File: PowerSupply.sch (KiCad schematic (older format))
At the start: 7 parts, among them P1 USB_OTG, P2 CONN_01X03, U1 LM3671MF-3.3

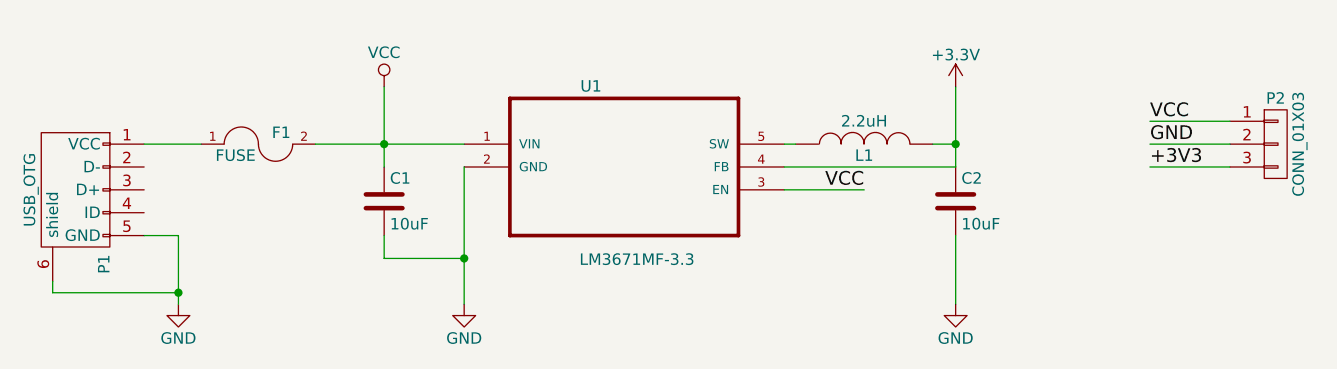
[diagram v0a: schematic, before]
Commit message: Adds Power-on LED
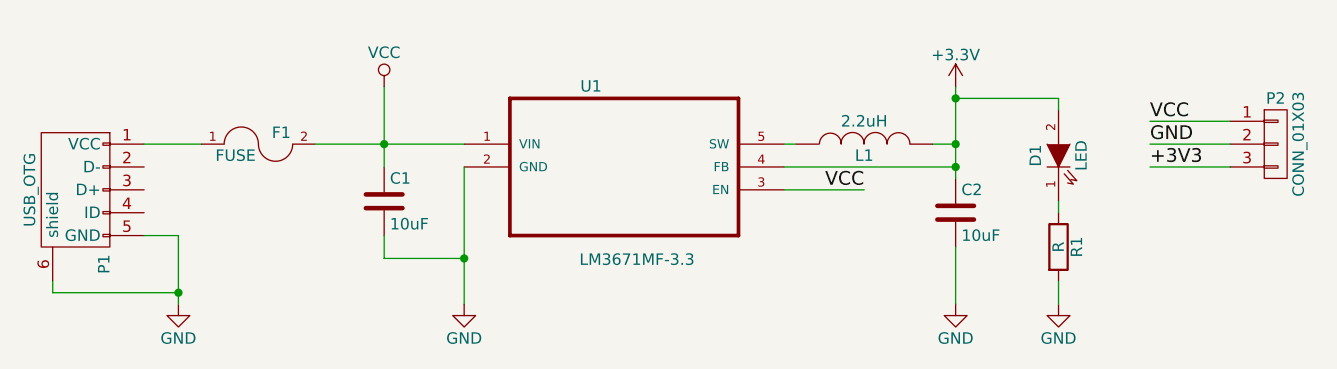
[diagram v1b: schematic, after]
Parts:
- added D1: LED, LEDs:LED_1206, symbol LED
- added R1: R, Resistors_SMD:R_1206_HandSoldering, symbol R
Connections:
- net +3V3: now also D1.2 (A)
- net GND: now also R1.2
- new net: D1.1 (K), R1.1
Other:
- moved on the sheet: C2
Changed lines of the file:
@@
 L C C2
 U 1 1 57CE1F50
-P 6750 2750
-F 0 "C2" H 6775 2850 50  0000 L CNN
-F 1 "10uF" H 6775 2650 50  0000 L CNN
-F 2 "Capacitors_SMD:C_1206_HandSoldering" H 6788 2600 50  0001 C CNN
-F 3 "" H 6750 2750 50  0000 C CNN
-	1    6750 2750
+P 6750 2800
+F 0 "C2" H 6775 2900 50  0000 L CNN
+F 1 "10uF" H 6775 2700 50  0000 L CNN
+F 2 "Capacitors_SMD:C_1206_HandSoldering" H 6788 2650 50  0001 C CNN
+F 3 "" H 6750 2800 50  0000 C CNN
+	1    6750 2800
 	1    0    0    -1
 $EndComp
@@
 	6000 2500 6050 2500
 Wire Wire Line
-	6650 2500 6750 2500
-Wire Wire Line
-	6750 2250 6750 2600
+	6750 2250 6750 2650
 Wire Wire Line
 	6750 2600 6000 2600
@@
 Connection ~ 6750 2500
 Wire Wire Line
-	6750 3200 6750 2900
+	6750 3200 6750 2950
 Wire Wire Line
 	3350 2900 3350 3200
@@
 Wire Wire Line
 	3950 2500 4600 2500
+$Comp
+L LED D1
+U 1 1 57DDBAF3
+P 7200 2550
+F 0 "D1" H 7200 2650 50  0000 C CNN
+F 1 "LED" H 7200 2450 50  0000 C CNN
+F 2 "LEDs:LED_1206" H 7200 2550 50  0001 C CNN
+F 3 "" H 7200 2550 50  0000 C CNN
+	1    7200 2550
+	0    -1   -1   0
+$EndComp
+$Comp
+L GND #PWR06
+U 1 1 57DDBCD9
+P 7200 3200
+F 0 "#PWR06" H 7200 2950 50  0001 C CNN
+F 1 "GND" H 7200 3050 50  0000 C CNN
+F 2 "" H 7200 3200 50  0000 C CNN
+F 3 "" H 7200 3200 50  0000 C CNN
+	1    7200 3200
+	1    0    0    -1
+$EndComp
+Connection ~ 6750 2600
+$Comp
+L R R1
+U 1 1 57DDC073
+P 7200 2950
+F 0 "R1" V 7280 2950 50  0000 C CNN
+F 1 "R" V 7200 2950 50  0000 C CNN
+F 2 "Resistors_SMD:R_1206_HandSoldering" V 7130 2950 50  0001 C CNN
+F 3 "" H 7200 2950 50  0000 C CNN
+	1    7200 2950
+	1    0    0    -1
+$EndComp
+Wire Wire Line
+	6650 2500 6750 2500
+Wire Wire Line
+	7200 2350 7200 2300
+Wire Wire Line
+	7200 2300 6750 2300
+Connection ~ 6750 2300
+Wire Wire Line
+	7200 2750 7200 2800
+Wire Wire Line
+	7200 3100 7200 3200
 $EndSCHEMATC

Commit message: Added updated schematic with L1 in 1008 package
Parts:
- L1: footprint Capacitors_SMD:C_0805_HandSoldering -> PowerSupply:C_1008_HandSoldering
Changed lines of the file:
@@
 F 0 "L1" V 6300 2500 50  0000 C CNN
 F 1 "2.2uH" V 6450 2500 50  0000 C CNN
-F 2 "Capacitors_SMD:C_0805_HandSoldering" H 6350 2500 50  0001 C CNN
+F 2 "PowerSupply:C_1008_HandSoldering" H 6350 2500 50  0001 C CNN
 F 3 "" H 6350 2500 50  0000 C CNN
 	1    6350 2500

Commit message: A lot of changes (BOM, layout, routing) Replaces inductor with footprint compatible with CDRH2D09 (Sumida) and NRH2412T (Taiyo Yuden) Removes access to 5V pin (replaced 3-pin connector with 2-pin) Updated layout, now more closely matching Adafruit's version of LM3671 breakout board, and following TI's layout example.
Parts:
- removed F1: FUSE, Fuse_Holders_and_Fuses:Fuse_SMD1206_Reflow, symbol FUSE
- C1, C2: footprint Capacitors_SMD:C_1206_HandSoldering -> Capacitors_SMD:C_1206
- L1: footprint PowerSupply:C_1008_HandSoldering -> Inductors:Inductor_Taiyo-Yuden_NR-24xx_HandSoldering
- P2: footprint Pin_Headers:Pin_Header_Straight_1x03 -> Pin_Headers:Pin_Header_Straight_1x02; symbol CONN_01X03 -> CONN_01X02
- R1: footprint Resistors_SMD:R_1206_HandSoldering -> Resistors_SMD:R_1206
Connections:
- net +3V3: now also P2.2 (P2); no longer P2.3 (P3)
- net GND: now also P2.1 (P1); no longer P2.2 (P2)
- net VCC: now also P1.1 (VCC); no longer P2.1 (P1)
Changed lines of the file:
@@
 F 0 "C1" H 4275 2850 50  0000 L CNN
 F 1 "10uF" H 4275 2650 50  0000 L CNN
-F 2 "Capacitors_SMD:C_1206_HandSoldering" H 4288 2600 50  0001 C CNN
+F 2 "Capacitors_SMD:C_1206" H 4288 2600 50  0001 C CNN
 F 3 "" H 4250 2750 50  0000 C CNN
 	1    4250 2750
@@
 F 0 "C2" H 6775 2900 50  0000 L CNN
 F 1 "10uF" H 6775 2700 50  0000 L CNN
-F 2 "Capacitors_SMD:C_1206_HandSoldering" H 6788 2650 50  0001 C CNN
+F 2 "Capacitors_SMD:C_1206" H 6788 2650 50  0001 C CNN
 F 3 "" H 6750 2800 50  0000 C CNN
 	1    6750 2800
@@
 F 0 "L1" V 6300 2500 50  0000 C CNN
 F 1 "2.2uH" V 6450 2500 50  0000 C CNN
-F 2 "PowerSupply:C_1008_HandSoldering" H 6350 2500 50  0001 C CNN
+F 2 "Inductors:Inductor_Taiyo-Yuden_NR-24xx_HandSoldering" H 6350 2500 50  0001 C CNN
 F 3 "" H 6350 2500 50  0000 C CNN
 	1    6350 2500
@@
 VCC
 $Comp
-L CONN_01X03 P2
+L CONN_01X02 P2
 U 1 1 57CEAA43
-P 8150 2500
-F 0 "P2" H 8150 2700 50  0000 C CNN
-F 1 "CONN_01X03" V 8250 2500 50  0000 C CNN
-F 2 "Pin_Headers:Pin_Header_Straight_1x03" H 8150 2500 50  0001 C CNN
-F 3 "" H 8150 2500 50  0000 C CNN
-	1    8150 2500
+P 8150 2550
+F 0 "P2" H 8150 2750 50  0000 C CNN
+F 1 "CONN_01X03" V 8250 2550 50  0000 C CNN
+F 2 "Pin_Headers:Pin_Header_Straight_1x02" H 8150 2550 50  0001 C CNN
+F 3 "" H 8150 2550 50  0000 C CNN
+	1    8150 2550
 	1    0    0    -1
 $EndComp
-Text Label 7600 2400 0    60   ~ 0
-VCC
 Text Label 7600 2500 0    60   ~ 0
 GND
@@
 	6000 2700 6350 2700
 Wire Wire Line
-	7950 2400 7600 2400
-Wire Wire Line
 	7950 2500 7600 2500
 Wire Wire Line
@@
 Text Label 7600 2600 0    60   ~ 0
 +3V3
-$Comp
-L FUSE F1
-U 1 1 57D06B4C
-P 3700 2500
-F 0 "F1" H 3800 2550 50  0000 C CNN
-F 1 "FUSE" H 3600 2450 50  0000 C CNN
-F 2 "Fuse_Holders_and_Fuses:Fuse_SMD1206_Reflow" H 3700 2500 50  0001 C CNN
-F 3 "" H 3700 2500 50  0000 C CNN
-	1    3700 2500
-	1    0    0    -1
-$EndComp
 Wire Wire Line
-	3450 2500 3200 2500
-Wire Wire Line
-	3950 2500 4600 2500
+	3200 2500 4600 2500
 $Comp
 L LED D1
@@
 F 0 "R1" V 7280 2950 50  0000 C CNN
 F 1 "R" V 7200 2950 50  0000 C CNN
-F 2 "Resistors_SMD:R_1206_HandSoldering" V 7130 2950 50  0001 C CNN
+F 2 "Resistors_SMD:R_1206" V 7130 2950 50  0001 C CNN
 F 3 "" H 7200 2950 50  0000 C CNN
 	1    7200 2950

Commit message: Updates orientation of Inductor (L1), and add test point for VCC)
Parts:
- added W1: TEST_1P, Pin_Headers:Pin_Header_Straight_1x01, symbol TEST_1P
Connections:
- net VCC: now also W1.1
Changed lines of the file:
@@
 Wire Wire Line
 	7200 3100 7200 3200
+$Comp
+L TEST_1P W1
+U 1 1 57F504C5
+P 8000 2100
+F 0 "W1" V 8000 2370 50  0000 C CNN
+F 1 "TEST_1P" V 7900 2250 50  0000 C CNN
+F 2 "Pin_Headers:Pin_Header_Straight_1x01" H 8200 2100 50  0001 C CNN
+F 3 "" H 8200 2100 50  0000 C CNN
+	1    8000 2100
+	0    1    1    0
+$EndComp
+Wire Wire Line
+	8000 2100 7600 2100
+Text Label 7600 2100 0    60   ~ 0
+VCC
 $EndSCHEMATC

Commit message: Updates value of C2 to 22 pF
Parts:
- C2: value 10uF -> 22uF
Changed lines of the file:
@@
 P 6750 2800
 F 0 "C2" H 6775 2900 50  0000 L CNN
-F 1 "10uF" H 6775 2700 50  0000 L CNN
+F 1 "22uF" H 6775 2700 50  0000 L CNN
 F 2 "Capacitors_SMD:C_1206" H 6788 2650 50  0001 C CNN
 F 3 "" H 6750 2800 50  0000 C CNN
